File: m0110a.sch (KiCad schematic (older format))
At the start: 14 parts

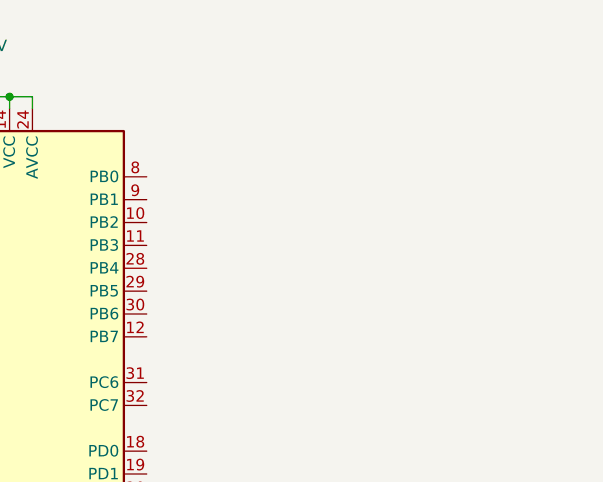
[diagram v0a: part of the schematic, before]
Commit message: Add USB to schematic
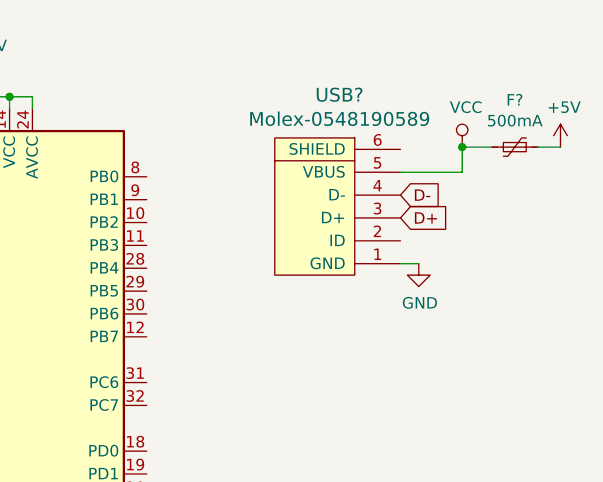
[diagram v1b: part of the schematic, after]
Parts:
- added F?: 500mA, symbol Device:Polyfuse_Small
- added USB?: Molex-0548190589, symbol random-keyboard-parts:Molex-0548190589
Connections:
- net +5V: now also F?.1
- net D+: now also USB?.3 (D+)
- net D-: now also USB?.4 (D-)
- net GND: now also USB?.1 (GND)
- new net VCC: F?.2, USB?.5 (VBUS)
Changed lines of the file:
@@
 Text GLabel 1450 2250 0    50   Input ~ 0
 D-
+$Comp
+L random-keyboard-parts:Molex-0548190589 USB?
+U 1 1 5F3D8139
+P 4210 1330
+F 0 "USB?" V 4747 1297 60  0000 C CNN
+F 1 "Molex-0548190589" V 4641 1297 60  0000 C CNN
+F 2 "" H 4210 1330 60  0001 C CNN
+F 3 "" H 4210 1330 60  0001 C CNN
+	1    4210 1330
+	0    -1   -1   0
+$EndComp
+$Comp
+L power:VCC #PWR?
+U 1 1 5F3D8CFB
+P 4780 1020
+F 0 "#PWR?" H 4780 870 50  0001 C CNN
+F 1 "VCC" H 4797 1193 50  0000 C CNN
+F 2 "" H 4780 1020 50  0001 C CNN
+F 3 "" H 4780 1020 50  0001 C CNN
+	1    4780 1020
+	1    0    0    -1
+$EndComp
+$Comp
+L Device:Polyfuse_Small F?
+U 1 1 5F3D911D
+P 5010 1020
+F 0 "F?" V 4805 1020 50  0000 C CNN
+F 1 "500mA" V 4896 1020 50  0000 C CNN
+F 2 "" H 5060 820 50  0001 L CNN
+F 3 "~" H 5010 1020 50  0001 C CNN
+	1    5010 1020
+	0    1    1    0
+$EndComp
+$Comp
+L power:+5V #PWR?
+U 1 1 5F3DA162
+P 5210 1020
+F 0 "#PWR?" H 5210 870 50  0001 C CNN
+F 1 "+5V" H 5225 1193 50  0000 C CNN
+F 2 "" H 5210 1020 50  0001 C CNN
+F 3 "" H 5210 1020 50  0001 C CNN
+	1    5210 1020
+	1    0    0    -1
+$EndComp
+Wire Wire Line
+	5210 1020 5110 1020
+Wire Wire Line
+	4910 1020 4780 1020
+Text GLabel 4510 1230 2    50   Input ~ 0
+D-
+Text GLabel 4510 1330 2    50   Input ~ 0
+D+
+$Comp
+L power:GND #PWR?
+U 1 1 5F3DECA5
+P 4590 1530
+F 0 "#PWR?" H 4590 1280 50  0001 C CNN
+F 1 "GND" H 4595 1357 50  0000 C CNN
+F 2 "" H 4590 1530 50  0001 C CNN
+F 3 "" H 4590 1530 50  0001 C CNN
+	1    4590 1530
+	1    0    0    -1
+$EndComp
+Wire Wire Line
+	4590 1530 4510 1530
+Wire Wire Line
+	4510 1130 4780 1130
+Wire Wire Line
+	4780 1130 4780 1020
+Connection ~ 4780 1020
 $EndSCHEMATC

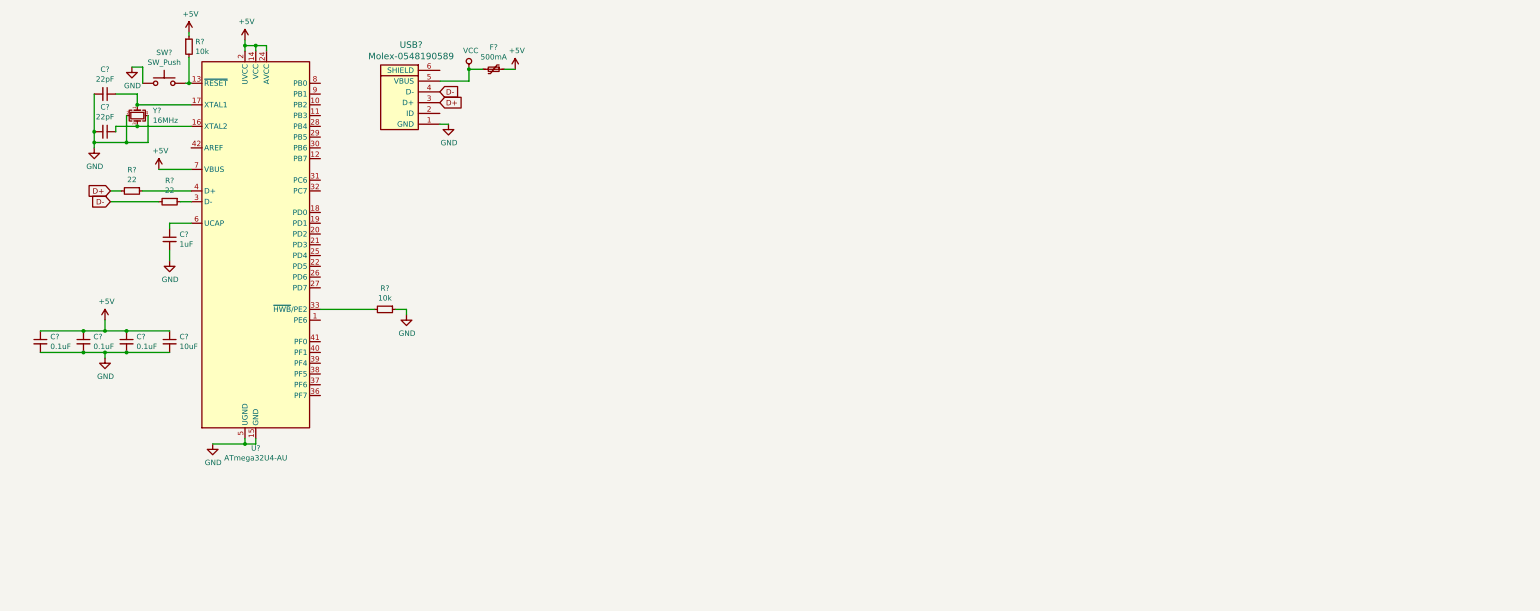
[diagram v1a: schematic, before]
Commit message: Add switches and diodes to schematic
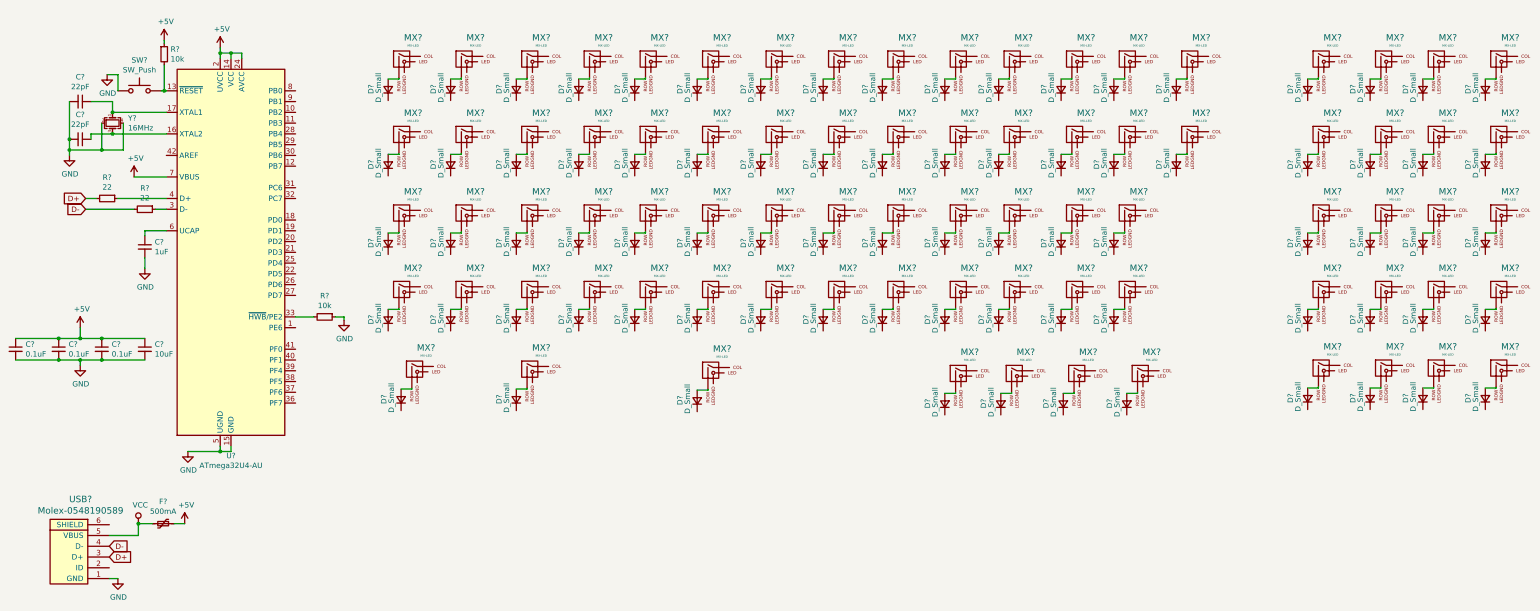
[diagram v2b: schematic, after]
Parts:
- added D? (x81): D_Small, symbol Device:D_Small
- added MX? (x81): MX-LED, symbol MX_Alps_Hybrid:MX-LED
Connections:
- new net: D?.2 (A), MX?.2 (ROW) (x81)
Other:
- moved on the sheet: C?, F?, R?, SW?, U?, USB?, Y?

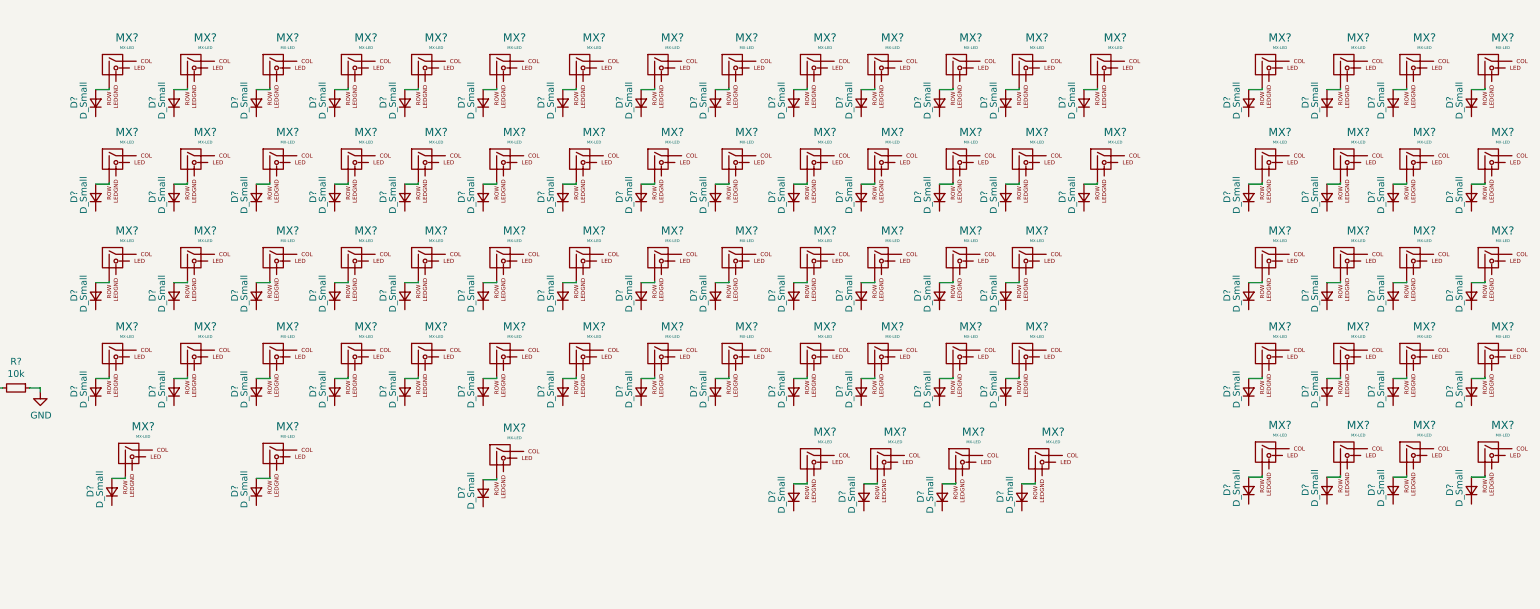
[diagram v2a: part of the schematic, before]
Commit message: Add matrix wiring to schematic
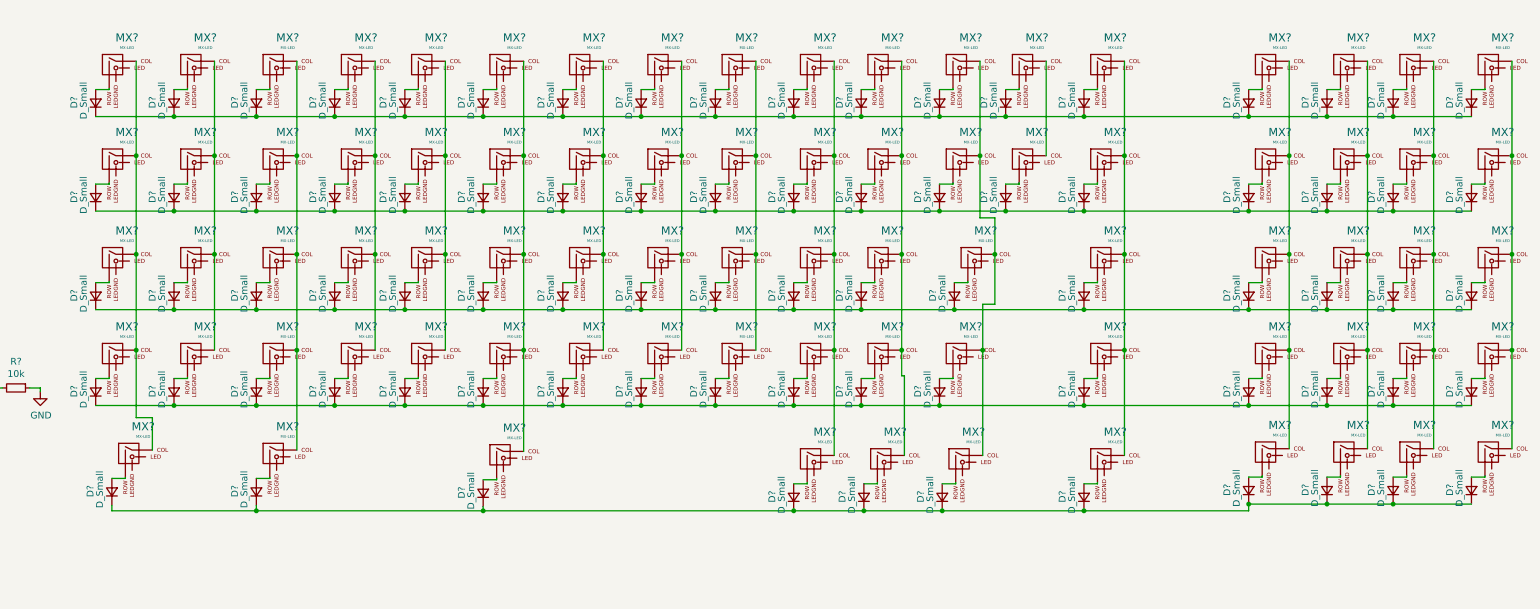
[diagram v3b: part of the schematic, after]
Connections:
- net at MX?.1 (COL): now also MX?.1 (COL), MX?.1 (COL), MX?.1 (COL), MX?.1 (COL) (x11)
- net at D?.1 (K): now also D?.1 (K), D?.1 (K), D?.1 (K), D?.1 (K), D?.1 (K), D?.1 (K), D?.1 (K), D?.1 (K), D?.1 (K), D?.1 (K), D?.1 (K), D?.1 (K), D?.1 (K), D?.1 (K), D?.1 (K), D?.1 (K), D?.1 (K) (x2)
- net at MX?.1 (COL): now also MX?.1 (COL), MX?.1 (COL), MX?.1 (COL) (x6)
- net at MX?.1 (COL): now also MX?.1 (COL)
- net at D?.1 (K): now also D?.1 (K), D?.1 (K), D?.1 (K), D?.1 (K), D?.1 (K), D?.1 (K), D?.1 (K), D?.1 (K), D?.1 (K), D?.1 (K), D?.1 (K), D?.1 (K), D?.1 (K), D?.1 (K), D?.1 (K), D?.1 (K) (x2)
- net at D?.1 (K): now also D?.1 (K), D?.1 (K), D?.1 (K), D?.1 (K), D?.1 (K), D?.1 (K), D?.1 (K), D?.1 (K), D?.1 (K), D?.1 (K)
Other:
- moved on the sheet: D?, MX?

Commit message: add row and colum globals
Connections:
- net COL0: now reaches MX?.1 (COL), MX?.1 (COL), MX?.1 (COL), MX?.1 (COL), MX?.1 (COL)
- net ROW0: now reaches D?.1 (K), D?.1 (K), D?.1 (K), D?.1 (K), D?.1 (K), D?.1 (K), D?.1 (K), D?.1 (K), D?.1 (K), D?.1 (K), D?.1 (K), D?.1 (K), D?.1 (K), D?.1 (K), D?.1 (K), D?.1 (K), D?.1 (K), D?.1 (K)
- net COL1: now reaches MX?.1 (COL), MX?.1 (COL), MX?.1 (COL), MX?.1 (COL)
- net COL3: now reaches MX?.1 (COL), MX?.1 (COL), MX?.1 (COL), MX?.1 (COL)
- net COL2: now reaches MX?.1 (COL), MX?.1 (COL), MX?.1 (COL), MX?.1 (COL), MX?.1 (COL)
- net COL5: now reaches MX?.1 (COL), MX?.1 (COL), MX?.1 (COL), MX?.1 (COL), MX?.1 (COL)
- net COL4: now reaches MX?.1 (COL), MX?.1 (COL), MX?.1 (COL), MX?.1 (COL)
- net COL7: now reaches MX?.1 (COL), MX?.1 (COL), MX?.1 (COL), MX?.1 (COL)
- net COL6: now reaches MX?.1 (COL), MX?.1 (COL), MX?.1 (COL), MX?.1 (COL)
- net COL9: now reaches MX?.1 (COL), MX?.1 (COL), MX?.1 (COL), MX?.1 (COL), MX?.1 (COL)
- net COL8: now reaches MX?.1 (COL), MX?.1 (COL), MX?.1 (COL), MX?.1 (COL)
- net COL11: now reaches MX?.1 (COL), MX?.1 (COL), MX?.1 (COL), MX?.1 (COL), MX?.1 (COL)
- net COL10: now reaches MX?.1 (COL), MX?.1 (COL), MX?.1 (COL), MX?.1 (COL), MX?.1 (COL)
- net COL13: now reaches MX?.1 (COL), MX?.1 (COL), MX?.1 (COL), MX?.1 (COL), MX?.1 (COL)
- net COL12: now reaches MX?.1 (COL), MX?.1 (COL)
- net COL15: now reaches MX?.1 (COL), MX?.1 (COL), MX?.1 (COL), MX?.1 (COL), MX?.1 (COL)
- net COL14: now reaches MX?.1 (COL), MX?.1 (COL), MX?.1 (COL), MX?.1 (COL), MX?.1 (COL)
- net COL17: now reaches MX?.1 (COL), MX?.1 (COL), MX?.1 (COL), MX?.1 (COL), MX?.1 (COL)
- net COL16: now reaches MX?.1 (COL), MX?.1 (COL), MX?.1 (COL), MX?.1 (COL), MX?.1 (COL)
- net ROW1: now reaches D?.1 (K), D?.1 (K), D?.1 (K), D?.1 (K), D?.1 (K), D?.1 (K), D?.1 (K), D?.1 (K), D?.1 (K), D?.1 (K), D?.1 (K), D?.1 (K), D?.1 (K), D?.1 (K), D?.1 (K), D?.1 (K), D?.1 (K), D?.1 (K)
- net ROW2: now reaches D?.1 (K), D?.1 (K), D?.1 (K), D?.1 (K), D?.1 (K), D?.1 (K), D?.1 (K), D?.1 (K), D?.1 (K), D?.1 (K), D?.1 (K), D?.1 (K), D?.1 (K), D?.1 (K), D?.1 (K), D?.1 (K), D?.1 (K)
- net ROW3: now reaches D?.1 (K), D?.1 (K), D?.1 (K), D?.1 (K), D?.1 (K), D?.1 (K), D?.1 (K), D?.1 (K), D?.1 (K), D?.1 (K), D?.1 (K), D?.1 (K), D?.1 (K), D?.1 (K), D?.1 (K), D?.1 (K), D?.1 (K)
- net ROW4: now reaches D?.1 (K), D?.1 (K), D?.1 (K), D?.1 (K), D?.1 (K), D?.1 (K), D?.1 (K), D?.1 (K), D?.1 (K), D?.1 (K), D?.1 (K)
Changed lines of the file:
@@
 Connection ~ 11350 4230
 Connection ~ 12570 4180
+Wire Wire Line
+	4030 1310 3760 1310
+Connection ~ 4030 1310
+Wire Wire Line
+	4030 2010 3780 2010
+Connection ~ 4030 2010
+Wire Wire Line
+	4030 2740 3780 2740
+Connection ~ 4030 2740
+Wire Wire Line
+	4030 3450 3820 3450
+Connection ~ 4030 3450
+Wire Wire Line
+	4150 4230 3890 4230
+Connection ~ 4150 4230
+Text GLabel 3760 1310 0    50   Input ~ 0
+ROW0
+Text GLabel 3780 2010 0    50   Input ~ 0
+ROW1
+Text GLabel 3780 2740 0    50   Input ~ 0
+ROW2
+Text GLabel 3820 3450 3    50   Input ~ 0
+ROW3
+Text GLabel 3890 4230 0    50   Input ~ 0
+ROW4
+Connection ~ 4330 900
+Wire Wire Line
+	4910 900  4910 830
+Wire Wire Line
+	4910 830  4950 830
+Connection ~ 4910 900
+Wire Wire Line
+	4330 830  4390 830
+Wire Wire Line
+	4330 830  4330 900
+Wire Wire Line
+	5520 900  5520 830
+Wire Wire Line
+	5520 830  5580 830
+Connection ~ 5520 900
+Wire Wire Line
+	6100 900  6100 840
+Wire Wire Line
+	6100 840  6160 840
+Connection ~ 6100 900
+Wire Wire Line
+	6620 900  6620 840
+Wire Wire Line
+	6620 840  6690 840
+Connection ~ 6620 900
+Wire Wire Line
+	7200 900  7200 830
+Wire Wire Line
+	7200 830  7260 830
+Connection ~ 7200 900
+Wire Wire Line
+	7790 900  7790 840
+Wire Wire Line
+	7790 840  7850 840
+Connection ~ 7790 900
+Wire Wire Line
+	8370 900  8370 840
+Wire Wire Line
+	8370 840  8440 840
+Connection ~ 8370 900
+Wire Wire Line
+	8920 900  8920 840
+Wire Wire Line
+	8920 840  8990 840
+Connection ~ 8920 900
+Wire Wire Line
+	9500 900  9500 840
+Wire Wire Line
+	9500 840  9570 840
+Connection ~ 9500 900
+Wire Wire Line
+	10000 900  10000 840
+Wire Wire Line
+	10000 840  10090 840
+Connection ~ 10000 900
+Wire Wire Line
+	10580 900  10580 840
+Wire Wire Line
+	10580 840  10660 840
+Connection ~ 10580 900
+Wire Wire Line
+	11070 900  11070 840
+Wire Wire Line
+	11070 840  11140 840
+Connection ~ 11070 900
+Wire Wire Line
+	11650 900  11650 840
+Wire Wire Line
+	11650 840  11730 840
+Connection ~ 11650 900
+Wire Wire Line
+	12870 900  12870 830
+Wire Wire Line
+	12870 830  12960 830
+Connection ~ 12870 900
+Wire Wire Line
+	13450 900  13450 840
+Wire Wire Line
+	13450 840  13530 840
+Connection ~ 13450 900
+Wire Wire Line
+	13940 900  13940 850
+Wire Wire Line
+	13940 850  14010 850
+Connection ~ 13940 900
+Wire Wire Line
+	14520 900  14520 840
+Wire Wire Line
+	14520 840  14600 840
+Connection ~ 14520 900
+Text GLabel 4390 830  2    50   Input ~ 0
+COL0
+Text GLabel 4950 830  2    50   Input ~ 0
+COL1
+Text GLabel 5580 830  2    50   Input ~ 0
+COL2
+Text GLabel 6160 840  2    50   Input ~ 0
+COL3
+Text GLabel 6690 840  2    50   Input ~ 0
+COL4
+Text GLabel 7260 830  2    50   Input ~ 0
+COL5
+Text GLabel 7850 840  2    50   Input ~ 0
+COL6
+Text GLabel 8440 840  1    50   Input ~ 0
+COL7
+Text GLabel 8990 840  2    50   Input ~ 0
+COL8
+Text GLabel 9570 840  1    50   Input ~ 0
+COL9
+Text GLabel 10090 840  1    50   Input ~ 0
+COL10
+Text GLabel 10660 840  1    50   Input ~ 0
+COL11
+Text GLabel 11140 840  1    50   Input ~ 0
+COL12
+Text GLabel 11730 840  2    50   Input ~ 0
+COL13
+Text GLabel 12960 830  1    50   Input ~ 0
+COL14
+Text GLabel 13530 840  1    50   Input ~ 0
+COL15
+Text GLabel 14010 850  1    50   Input ~ 0
+COL16
+Text GLabel 14600 840  2    50   Input ~ 0
+COL17
 $EndSCHEMATC

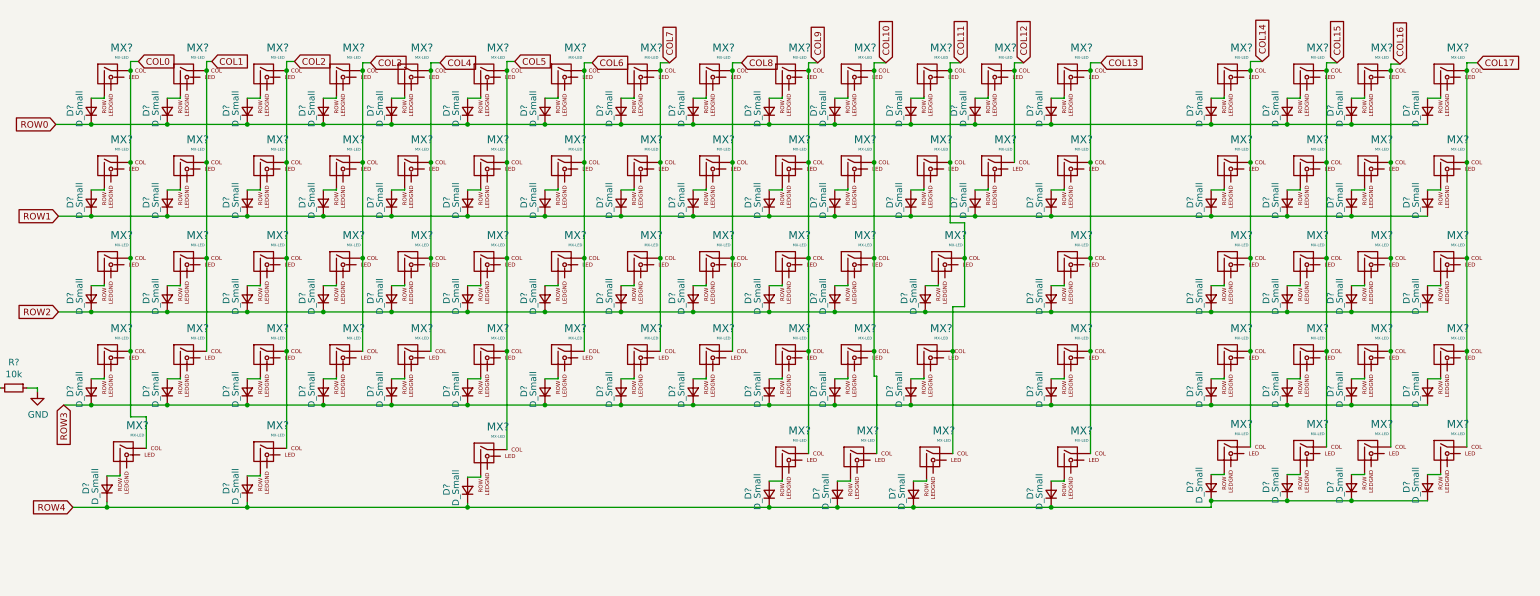
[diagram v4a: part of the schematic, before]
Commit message: added switch references
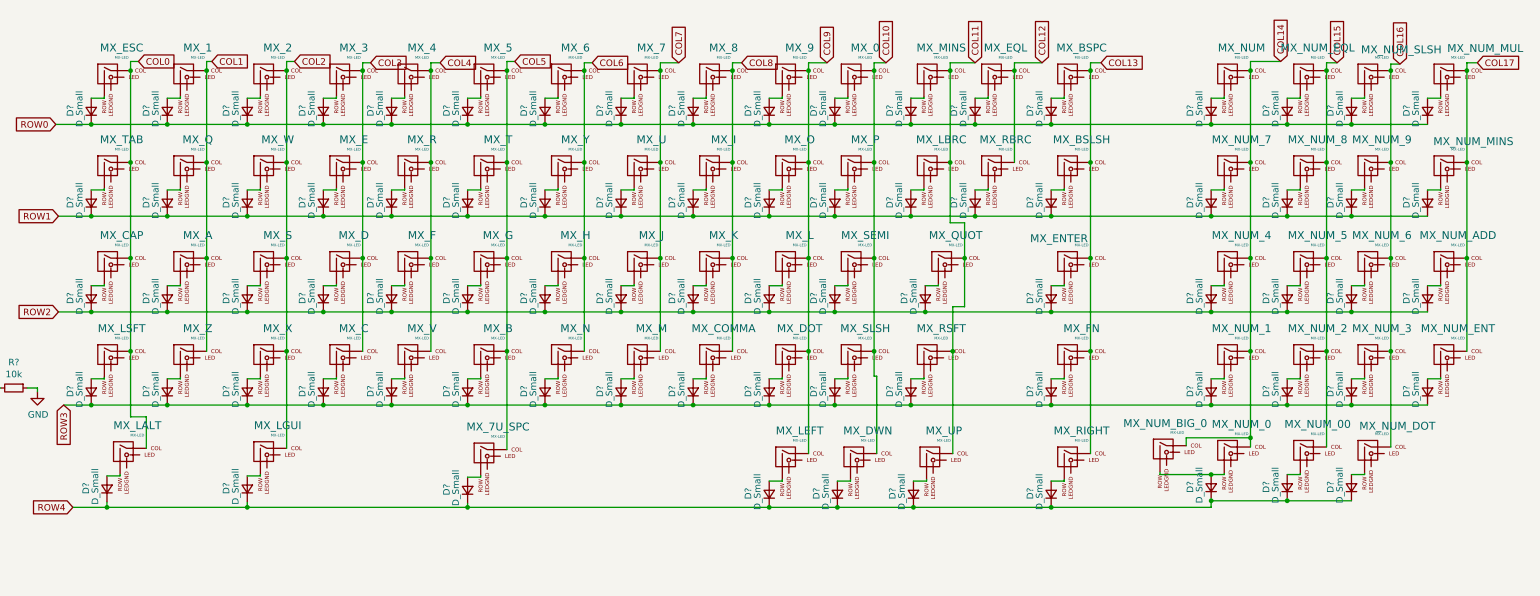
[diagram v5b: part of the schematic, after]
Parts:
- removed D?: D_Small, symbol Device:D_Small
- removed MX?: MX-LED, symbol MX_Alps_Hybrid:MX-LED
- added MX_NUM_BIG_0: MX-LED, symbol MX_Alps_Hybrid:MX-LED
- gave numbers to parts that had none: 80
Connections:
- net COL14: now also MX_NUM_BIG_0.1 (COL)
- net at D?.2 (A), MX_NUM_0.2 (ROW): now also MX_NUM_BIG_0.2 (ROW)
